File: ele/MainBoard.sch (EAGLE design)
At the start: 126 parts, among them IC1 MCP23017SP, IC2 74HC595D, IC3 74HC595D, X1 POWER_IN, X10 M7, X2 POWER_OUT, X3 M2, X4 M4, X5 M6, X6 M8, X7 M1, X8 M3, X9 M5

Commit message: ele: Previous changes routed into the PCB.
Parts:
- R2: value (none) -> 82k
- R3: value (none) -> 10k
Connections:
- net ENC7A: now also JP43.1; no longer JP43.2
- net PIEZO: now also JP43.2; no longer JP43.1
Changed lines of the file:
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@@
 <?xml version="1.0" encoding="utf-8"?>
 <!DOCTYPE eagle SYSTEM "eagle.dtd">
-<eagle version="9.0.0">
+<eagle version="9.0.1">
 <drawing>
 <settings>
@@
 <part name="+3V38" library="supply1" library_urn="urn:adsk.eagle:library:371" deviceset="+3V3" device=""/>
 <part name="GND17" library="supply1" library_urn="urn:adsk.eagle:library:371" deviceset="GND" device=""/>
-<part name="R2" library="resistor" library_urn="urn:adsk.eagle:library:348" deviceset="R-EU_" device="0204/2V" package3d_urn="urn:adsk.eagle:package:25948/1"/>
-<part name="R3" library="resistor" library_urn="urn:adsk.eagle:library:348" deviceset="R-EU_" device="0204/2V" package3d_urn="urn:adsk.eagle:package:25948/1"/>
+<part name="R2" library="resistor" library_urn="urn:adsk.eagle:library:348" deviceset="R-EU_" device="0204/2V" package3d_urn="urn:adsk.eagle:package:25948/1" value="82k"/>
+<part name="R3" library="resistor" library_urn="urn:adsk.eagle:library:348" deviceset="R-EU_" device="0204/2V" package3d_urn="urn:adsk.eagle:package:25948/1" value="10k"/>
 <part name="P+8" library="supply1" library_urn="urn:adsk.eagle:library:371" deviceset="VCC" device=""/>
 <part name="GND7" library="supply1" library_urn="urn:adsk.eagle:library:371" deviceset="GND" device=""/>
@@
 <instance part="PIEZO" gate="G$1" x="165.1" y="185.42" rot="MR0"/>
 <instance part="D2" gate="G$1" x="284.48" y="149.86" rot="R180"/>
-<instance part="JP43" gate="G$1" x="180.34" y="180.34" smashed="yes" rot="MR270">
-<attribute name="NAME" x="183.896" y="185.42" size="1.778" layer="95" rot="MR180"/>
-<attribute name="VALUE" x="183.896" y="182.88" size="1.778" layer="96" rot="MR180"/>
+<instance part="JP43" gate="G$1" x="177.8" y="180.34" smashed="yes" rot="R270">
+<attribute name="NAME" x="174.244" y="185.42" size="1.778" layer="95" rot="R180"/>
+<attribute name="VALUE" x="174.244" y="182.88" size="1.778" layer="96" rot="R180"/>
 </instance>
 </instances>
@@
 <pinref part="RN5" gate="B" pin="1"/>
 <wire x1="223.52" y1="187.96" x2="180.34" y2="187.96" width="0.1524" layer="91"/>
-<pinref part="JP43" gate="G$1" pin="2"/>
+<pinref part="JP43" gate="G$1" pin="1"/>
 <wire x1="180.34" y1="187.96" x2="180.34" y2="182.88" width="0.1524" layer="91"/>
 </segment>
@@
 <pinref part="PIEZO" gate="G$1" pin="-"/>
 <wire x1="177.8" y1="187.96" x2="170.18" y2="187.96" width="0.1524" layer="91"/>
-<pinref part="JP43" gate="G$1" pin="1"/>
+<pinref part="JP43" gate="G$1" pin="2"/>
 <wire x1="177.8" y1="182.88" x2="177.8" y2="187.96" width="0.1524" layer="91"/>
 </segment>

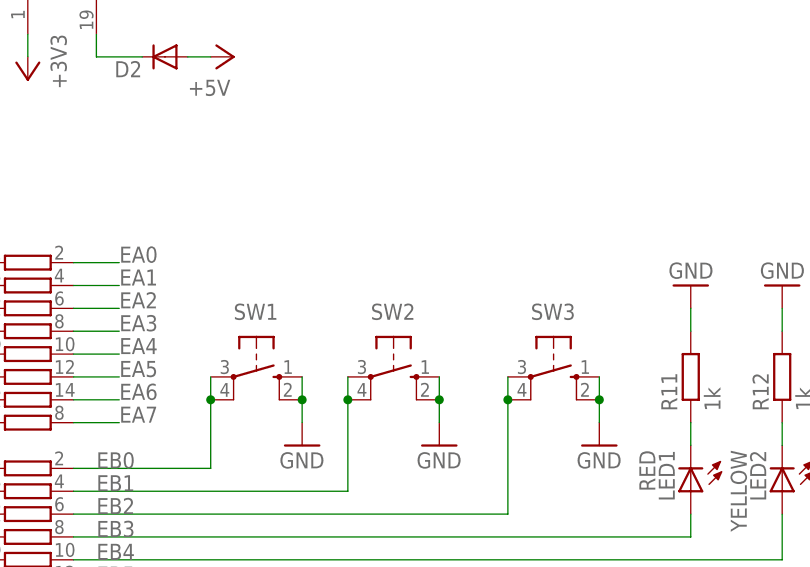
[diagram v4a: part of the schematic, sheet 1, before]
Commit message: ele: Added capacitors to buttons, added description to resistor arrays.
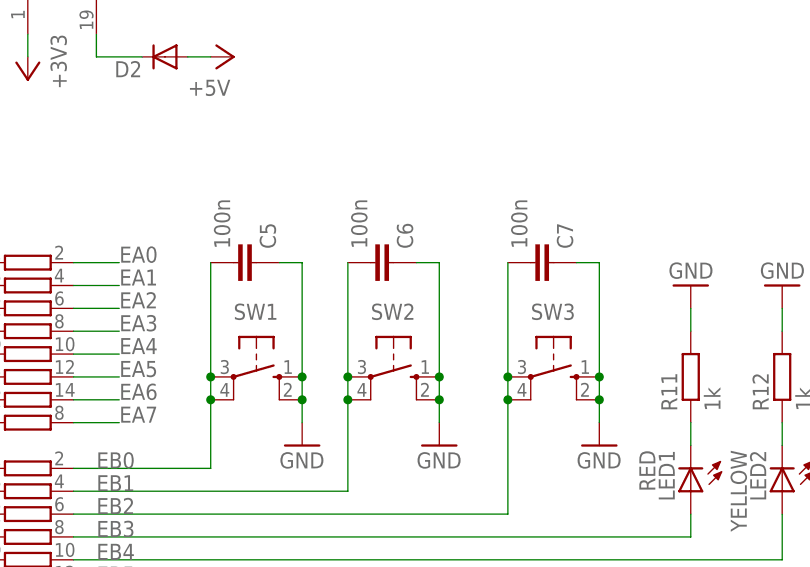
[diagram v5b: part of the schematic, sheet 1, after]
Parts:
- added C5, C6, C7: 100n, rcl_upravena:C-EUC1206
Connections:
- net EB0: now also C5.2
- net EB1: now also C6.2
- net EB2: now also C7.2
- net GND: now also C5.1, C6.1, C7.1
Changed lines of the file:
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@@
 <part name="R20" library="rcl_upravena" deviceset="R-EU_" device="0204/2V" value="10k"/>
 <part name="+3V4" library="supply1" library_urn="urn:adsk.eagle:library:371" deviceset="+3V3" device=""/>
+<part name="C5" library="rcl_upravena" deviceset="C-EU" device="C1206" value="100n"/>
+<part name="C6" library="rcl_upravena" deviceset="C-EU" device="C1206" value="100n"/>
+<part name="C7" library="rcl_upravena" deviceset="C-EU" device="C1206" value="100n"/>
 </parts>
 <sheets>
@@
 <attribute name="VALUE" x="174.244" y="182.88" size="1.778" layer="96" rot="R180"/>
 </instance>
+<instance part="C5" gate="G$1" x="294.64" y="127" rot="MR90"/>
+<instance part="C6" gate="G$1" x="309.88" y="127" rot="MR90"/>
+<instance part="C7" gate="G$1" x="327.66" y="127" rot="MR90"/>
 </instances>
 <busses>
@@
 <junction x="299.72" y="111.76"/>
 <wire x1="299.72" y1="111.76" x2="299.72" y2="109.22" width="0.1524" layer="91"/>
+<pinref part="C5" gate="G$1" pin="1"/>
+<wire x1="297.18" y1="127" x2="299.72" y2="127" width="0.1524" layer="91"/>
+<wire x1="299.72" y1="127" x2="299.72" y2="114.3" width="0.1524" layer="91"/>
+<junction x="299.72" y="114.3"/>
 </segment>
 <segment>
@@
 <junction x="314.96" y="111.76"/>
 <wire x1="314.96" y1="111.76" x2="314.96" y2="109.22" width="0.1524" layer="91"/>
+<pinref part="C6" gate="G$1" pin="1"/>
+<wire x1="312.42" y1="127" x2="314.96" y2="127" width="0.1524" layer="91"/>
+<wire x1="314.96" y1="127" x2="314.96" y2="114.3" width="0.1524" layer="91"/>
+<junction x="314.96" y="114.3"/>
 </segment>
 <segment>
@@
 <wire x1="332.74" y1="111.76" x2="332.74" y2="109.22" width="0.1524" layer="91"/>
 <junction x="332.74" y="111.76"/>
+<pinref part="C7" gate="G$1" pin="1"/>
+<wire x1="330.2" y1="127" x2="332.74" y2="127" width="0.1524" layer="91"/>
+<wire x1="332.74" y1="127" x2="332.74" y2="114.3" width="0.1524" layer="91"/>
+<junction x="332.74" y="114.3"/>
 </segment>
 <segment>
@@
 <label x="276.86" y="104.14" size="1.778" layer="95"/>
 <pinref part="RN2" gate="A" pin="2"/>
+<pinref part="C5" gate="G$1" pin="2"/>
+<wire x1="289.56" y1="127" x2="289.56" y2="114.3" width="0.1524" layer="91"/>
+<junction x="289.56" y="114.3"/>
 </segment>
 <segment>
@@
 <label x="276.86" y="101.6" size="1.778" layer="95"/>
 <pinref part="RN2" gate="B" pin="2"/>
+<pinref part="C6" gate="G$1" pin="2"/>
+<wire x1="304.8" y1="127" x2="304.8" y2="114.3" width="0.1524" layer="91"/>
+<junction x="304.8" y="114.3"/>
 </segment>
 <segment>
@@
 <pinref part="SW3" gate="1" pin="P1"/>
 <junction x="322.58" y="111.76"/>
+<pinref part="C7" gate="G$1" pin="2"/>
+<wire x1="322.58" y1="127" x2="322.58" y2="114.3" width="0.1524" layer="91"/>
+<junction x="322.58" y="114.3"/>
 </segment>
 <segment>

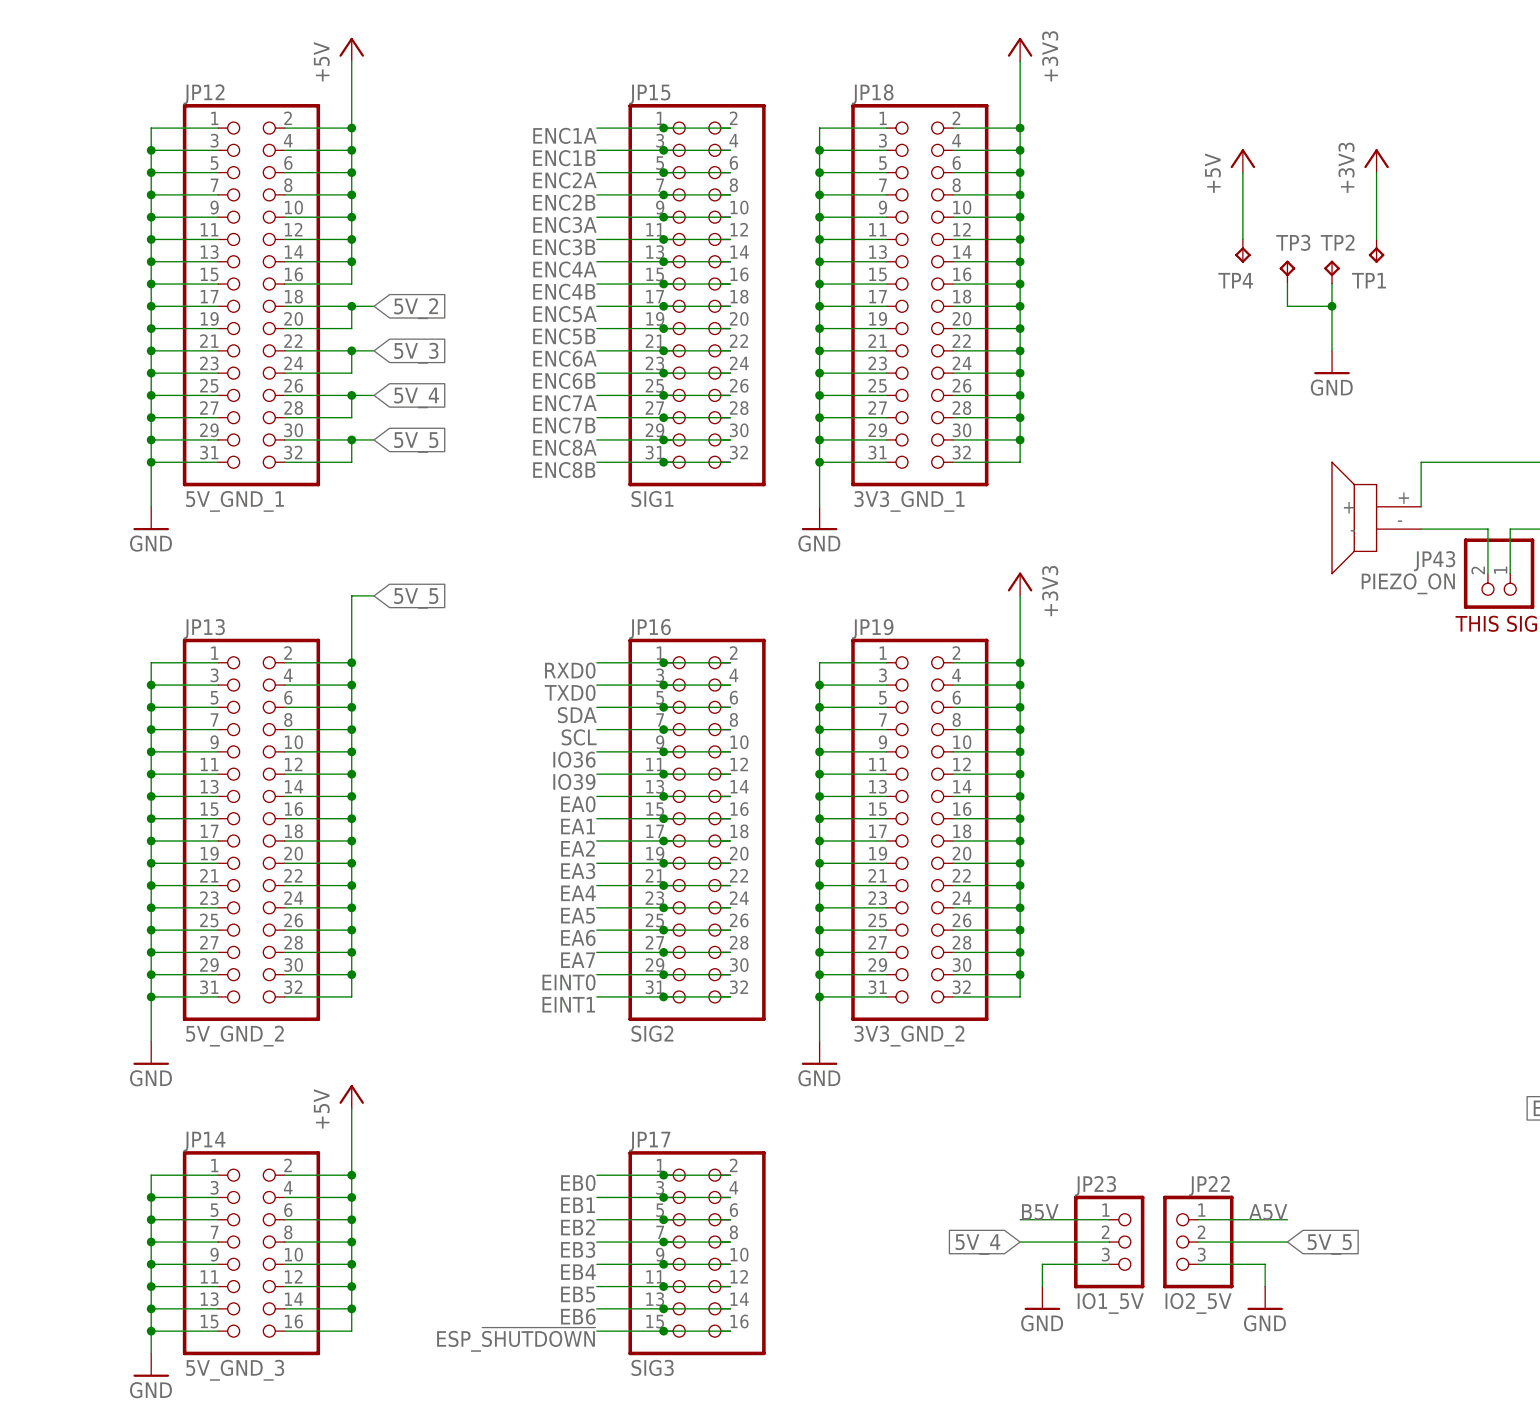
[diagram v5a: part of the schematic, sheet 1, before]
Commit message: ele: MainBoard - fix bug with stepdowns - reroute all routes from stepdowns (please check @cednik)
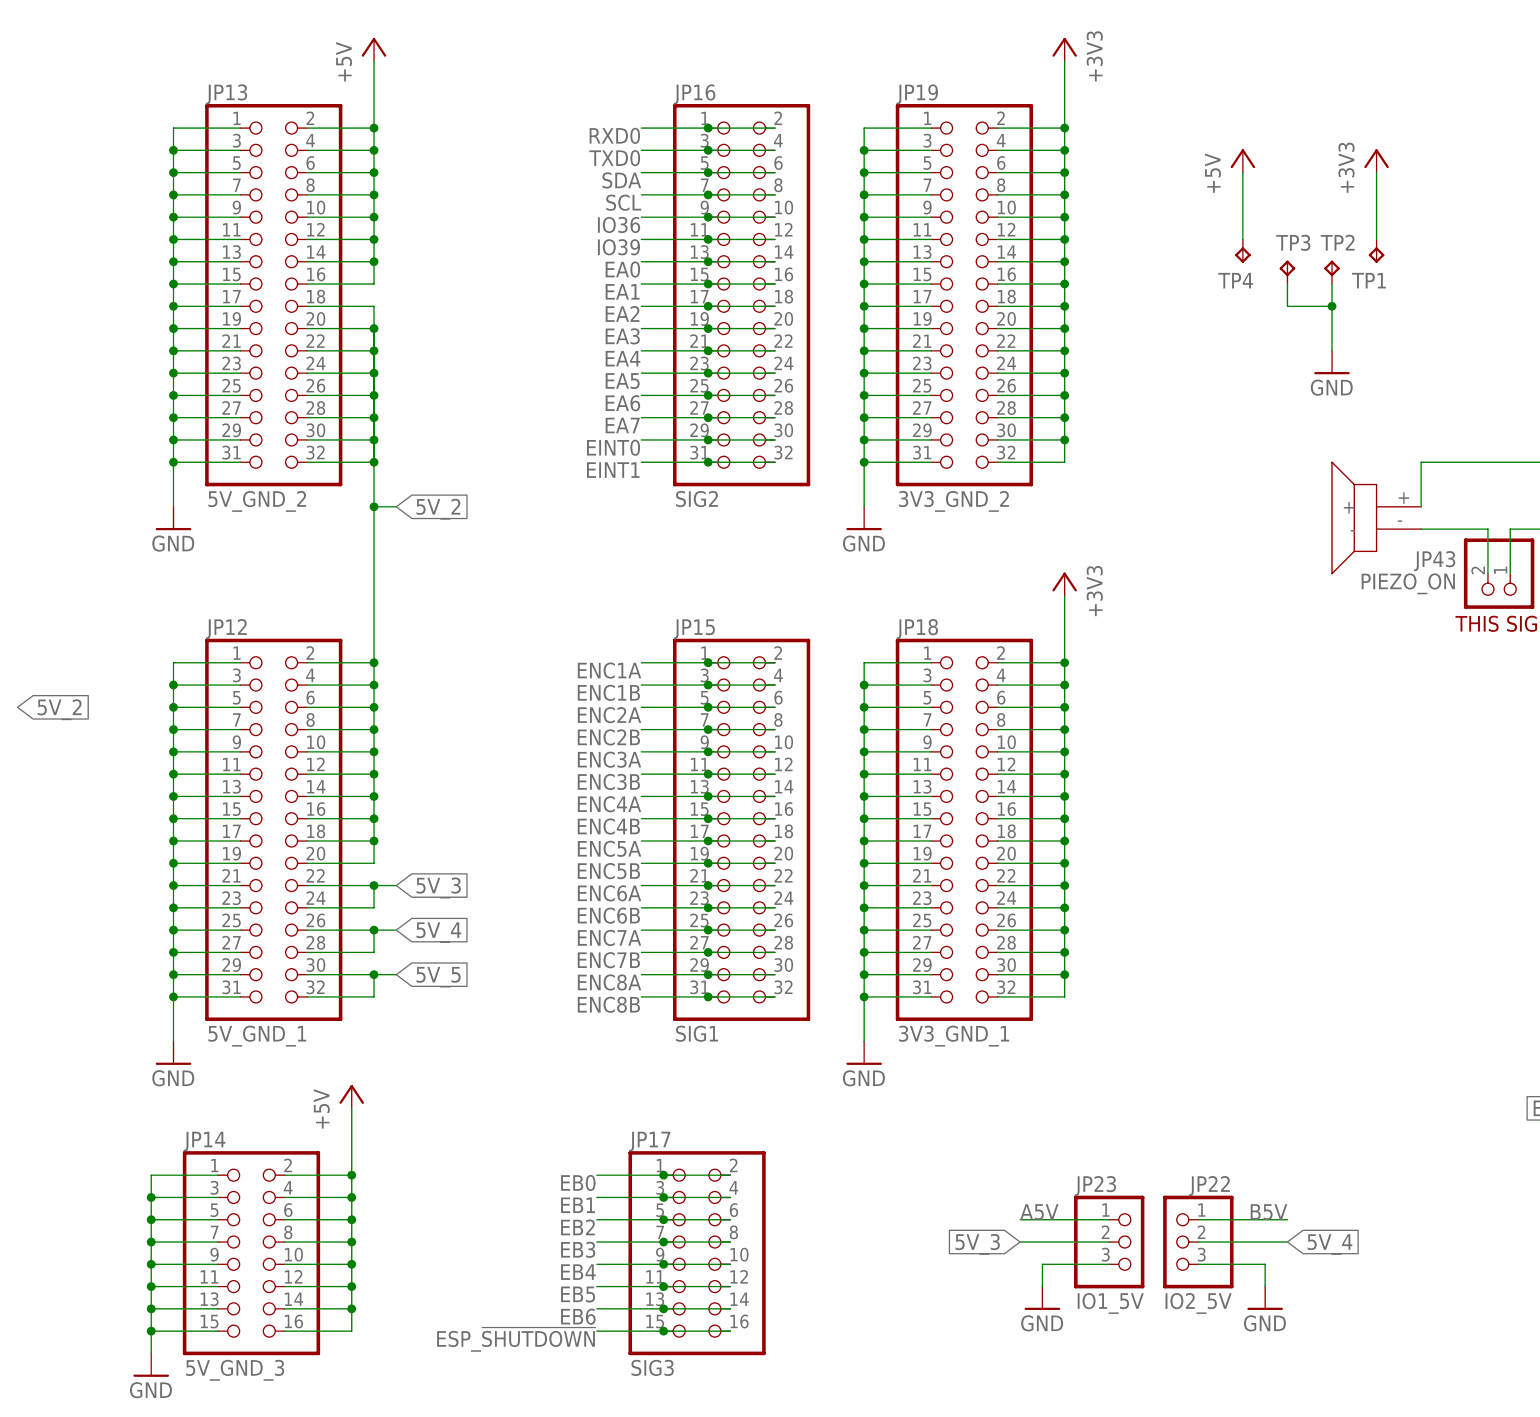
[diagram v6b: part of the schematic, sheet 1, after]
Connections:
- net N$2 renamed STEP2_EN
- net N$5 renamed STEP3_EN
- net N$7 renamed STEP4_EN
- net N$8 renamed STEP5_EN
- net +5V: now also JP13.10, JP13.12, JP13.14, JP13.16, JP13.2, JP13.4, JP13.6, JP13.8; no longer JP12.10, JP12.12, JP12.14, JP12.16, JP12.2, JP12.4, JP12.6, JP12.8
- net 5V_2: now also JP12.10, JP12.12, JP12.14, JP12.16, JP12.2, JP12.4, JP12.6, JP12.8, JP13.18, JP13.20, JP13.22, JP13.24, JP13.26, JP13.28, JP13.30, JP13.32
- net 5V_3: now also JP23.2
- net 5V_4: now also JP22.2; no longer JP23.2
- net 5V_5: no longer JP13.10, JP13.12, JP13.14, JP13.16, JP13.18, JP13.2, JP13.20, JP13.22, JP13.24, JP13.26, JP13.28, JP13.30, JP13.32, JP13.4, JP13.6, JP13.8, JP22.2
- net A5V: now also JP23.1; no longer JP22.1
- net B5V: now also JP22.1; no longer JP23.1
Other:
- moved on the sheet: JP12, JP13, JP15, JP16, JP18, JP19
